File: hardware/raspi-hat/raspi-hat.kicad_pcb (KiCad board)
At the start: 2 copper layers, 41 parts, among them J1 Conn_02x05_Counter_Clockwise, J3 ATX-20, Q1 FDMS86101DC, Q2 FDMS86101DC, Q3 FDMS86101DC, Q4 FDMS86101DC, Q5 FDMS86101DC, Q6 FDMS86101DC, U1 STSPIN32G4, Y1 Crystal_GND23_Small

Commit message: updatd ioc
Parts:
- removed Q6: FDMS86101DC, Package_DFN_QFN:PQFN-8-EP_6x5mm_P1.27mm_Generic
- added D3: ER1Q-LTP, Diode_SMD:D_SMB, F.Cu at (43.3, 37.7)
- added J2: Conn_01x03_Pin, Connector_Phoenix_MC:PhoenixContact_MC_1,5_3-G-3.81_1x03_P3.81mm_Horizontal, F.Cu at (102.9, 124.7)
- added J4: Raspberry_Pi_4, Connector_PinSocket_2.54mm:PinSocket_2x20_P2.54mm_Vertical, B.Cu at (108.2, 105.0)
- added Q7: FDMS86101, Package_TO_SOT_SMD:TDSON-8-1, F.Cu at (120.0, 122.0)
- added R23: 0, Resistor_SMD:R_0603_1608Metric, F.Cu at (41.1, 41.7)
- added R24: 0, Resistor_SMD:R_0603_1608Metric, F.Cu at (41.1, 44.2)
- added REF**: MountingHole_3.2mm_M3, MountingHole:MountingHole_3.2mm_M3, F.Cu at (161.5, 152.8)
- added REF**: MountingHole_3.2mm_M3, MountingHole:MountingHole_3.2mm_M3, F.Cu at (161.5, 103.8)
- added REF**: MountingHole_3.2mm_M3, MountingHole:MountingHole_3.2mm_M3, F.Cu at (103.5, 103.8)
- added REF**: MountingHole_3.2mm_M3, MountingHole:MountingHole_3.2mm_M3, F.Cu at (103.5, 152.5)
- added RV1: 10k, Potentiometer_SMD:Potentiometer_Bourns_3224W_Vertical, F.Cu at (71.0, 123.0)
- Q1, Q2, Q3, Q4, Q5: value FDMS86101DC -> FDMS86101; footprint Package_DFN_QFN:PQFN-8-EP_6x5mm_P1.27mm_Generic -> Package_TO_SOT_SMD:TDSON-8-1
- moved Q2 108.3 mm to (120.0, 136.0), turned to 0 degrees
- moved Q3 105.5 mm to (112.0, 136.0), turned to 0 degrees
- moved Q1 103.7 mm to (120.0, 129.0), turned to 0 degrees
- moved Q4 95.8 mm to (112.0, 129.0), turned to 0 degrees
- moved C5 88.7 mm to (59.5, 72.5)
- moved C1 88.7 mm to (56.2, 96.5)
- moved C2 88.7 mm to (52.2, 92.5)
- moved C3 88.7 mm to (88.2, 78.0)
- moved C4 88.7 mm to (88.2, 80.5)
- moved C6 88.7 mm to (62.9, 72.5)
- moved C7 88.7 mm to (66.2, 72.5)
- moved C8 88.7 mm to (84.2, 100.5)
- moved D1 88.7 mm to (92.2, 79.5)
- moved J1 88.7 mm to (65.2, 102.5)
- moved R1 88.7 mm to (73.2, 48.5)
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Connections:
- net /controller/+3V3 renamed /+3V3
- C5 pad 2: /controller/inverter/OUT1 -> /controller/phase_u
- C6 pad 2: /controller/inverter/OUT3 -> /controller/phase_w
- C7 pad 2: /controller/inverter/OUT2 -> /controller/phase_v
- J1 pad 10: unconnected-(J1-Pin_10-Pad10) -> /controller/reset
- J1 pad 2: unconnected-(J1-Pin_2-Pad2) -> /controller/v_mc
- J1 pad 4: unconnected-(J1-Pin_4-Pad4) -> /controller/v_mc
- J1 pad 5: unconnected-(J1-Pin_5-Pad5) -> /controller/swd_io
- J1 pad 7: unconnected-(J1-Pin_7-Pad7) -> /controller/swd_clk
- J1 pad 9: unconnected-(J1-Pin_9-Pad9) -> /GND
- J3 pad 14: /power-supply/pwr_on -> /GND
- Q1 pad 1: /controller/inverter/OUT1 -> /controller/phase_v
- Q1 pad 2: /controller/inverter/LS1 -> /controller/phase_v
- Q1 pad 3: Net-(Q1-S) -> /controller/phase_v
- Q1 pad 4: (no net) -> /controller/inverter/HS2
- Q1 pad 5: (no net) -> /+12V
- Q2 pad 1: /controller/inverter/OUT2 -> /controller/phase_w
- Q2 pad 2: /controller/inverter/LS2 -> /controller/phase_w
- Q2 pad 3: Net-(Q2-S) -> /controller/phase_w
- Q2 pad 4: (no net) -> /controller/inverter/HS3
- Q2 pad 5: (no net) -> /+12V
- Q3 pad 1: /controller/inverter/OUT3 -> Net-(Q3-S-Pad1)
- Q3 pad 2: /controller/inverter/LS3 -> Net-(Q3-S-Pad1)
- Q3 pad 3: Net-(Q3-S) -> Net-(Q3-S-Pad1)
- Q3 pad 4: (no net) -> /controller/inverter/LS3
- Q3 pad 5: (no net) -> /controller/phase_w
- Q4 pad 1: /controller/+12V -> Net-(Q4-S-Pad1)
- Q4 pad 2: /controller/inverter/HS3 -> Net-(Q4-S-Pad1)
- Q4 pad 3: /controller/inverter/OUT3 -> Net-(Q4-S-Pad1)
- Q4 pad 4: (no net) -> /controller/inverter/LS2
- Q4 pad 5: (no net) -> /controller/phase_v
- Q5 pad 1: /controller/+12V -> Net-(Q5-S-Pad1)
- Q5 pad 2: /controller/inverter/HS2 -> Net-(Q5-S-Pad1)
- Q5 pad 3: /controller/inverter/OUT2 -> Net-(Q5-S-Pad1)
- Q5 pad 4: (no net) -> /controller/inverter/LS1
- Q5 pad 5: (no net) -> /controller/phase_u
- R1 pad 4: Net-(Q1-S) -> Net-(Q5-S-Pad1)
- R2 pad 4: Net-(Q2-S) -> Net-(Q4-S-Pad1)
- R21 pad 1: /controller/+12V -> /+12V
- R3 pad 4: Net-(Q3-S) -> Net-(Q3-S-Pad1)
- U1 pad 36: /controller/inverter/OUT3 -> /controller/phase_w
- U1 pad 39: /controller/inverter/OUT2 -> /controller/phase_v
- U1 pad 42: /controller/inverter/OUT1 -> /controller/phase_u
- U1 pad 45: unconnected-(U1-PA9-Pad45) -> /controller/uart_tx
- U1 pad 46: unconnected-(U1-PA10-Pad46) -> /controller/uart_rx
- U1 pad 49: unconnected-(U1-PA13-Pad49) -> /controller/swd_io
- U1 pad 50: unconnected-(U1-PA14-Pad50) -> /controller/swd_clk
- U1 pad 52: unconnected-(U1-SCREF-Pad52) -> Net-(U1-SCREF)
- U1 pad 53: /controller/pwr_on -> unconnected-(U1-PD2-Pad53)
- U1 pad 59: /controller/i2c_scl -> /controller/boot
- U1 pad 60: /controller/i2c_sda -> unconnected-(U1-PB9-Pad60)
- U1 pad 61: /controller/+12V -> /+12V
- U1 pad 64: /controller/+12V -> /+12V
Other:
- board outline added: 65 x 57 mm

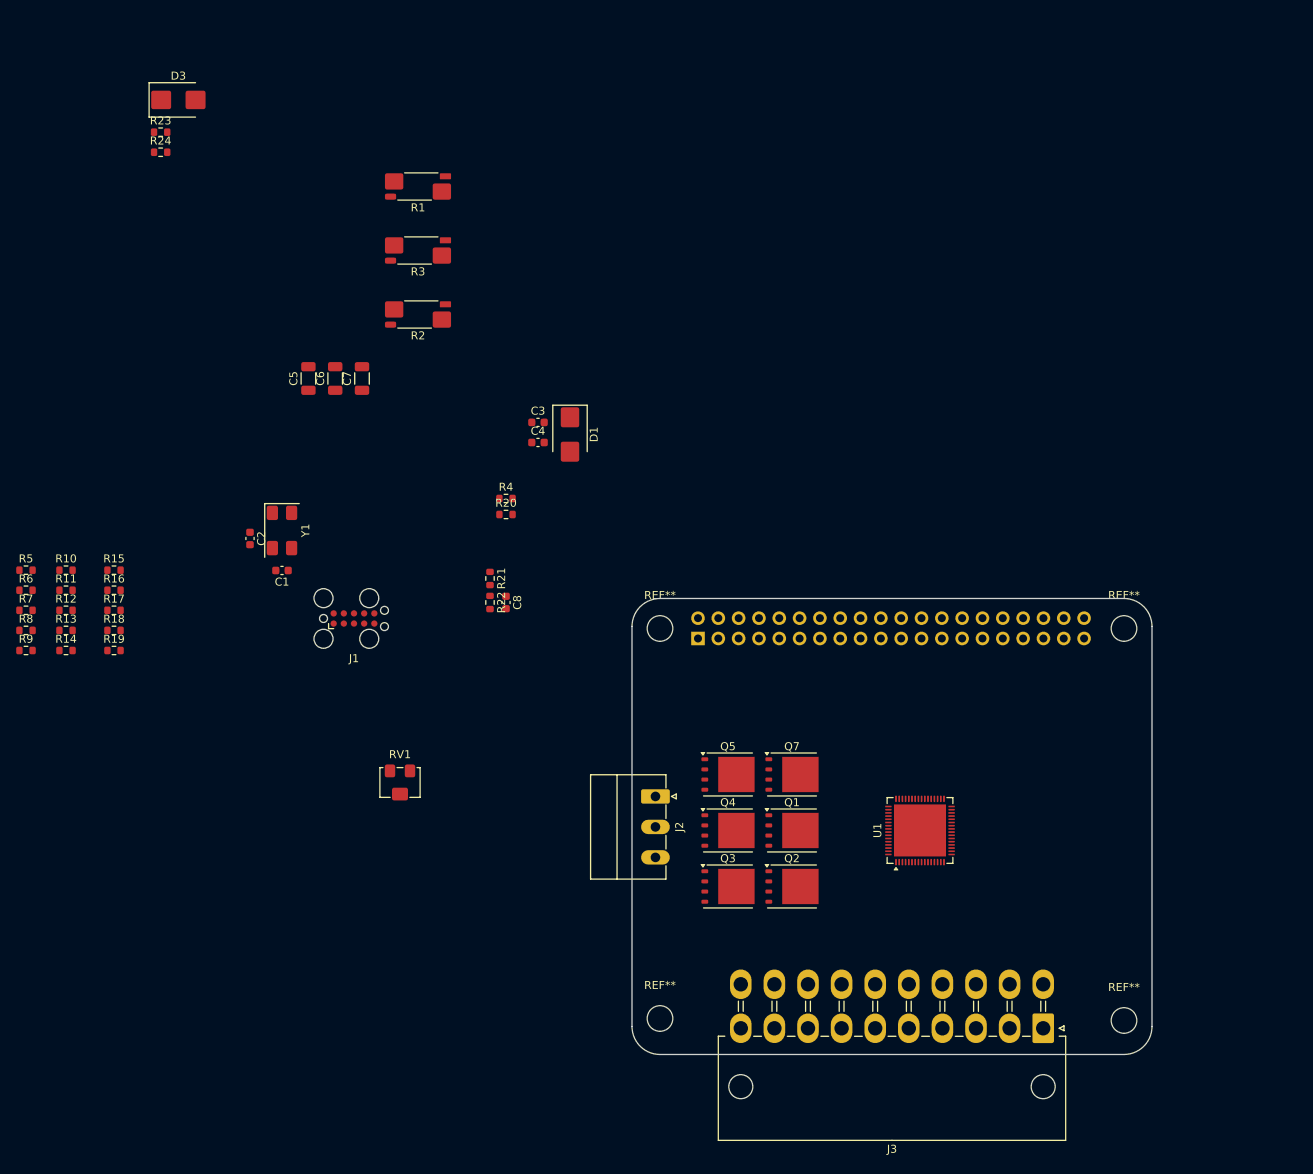
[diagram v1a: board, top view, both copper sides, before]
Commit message: added more parts
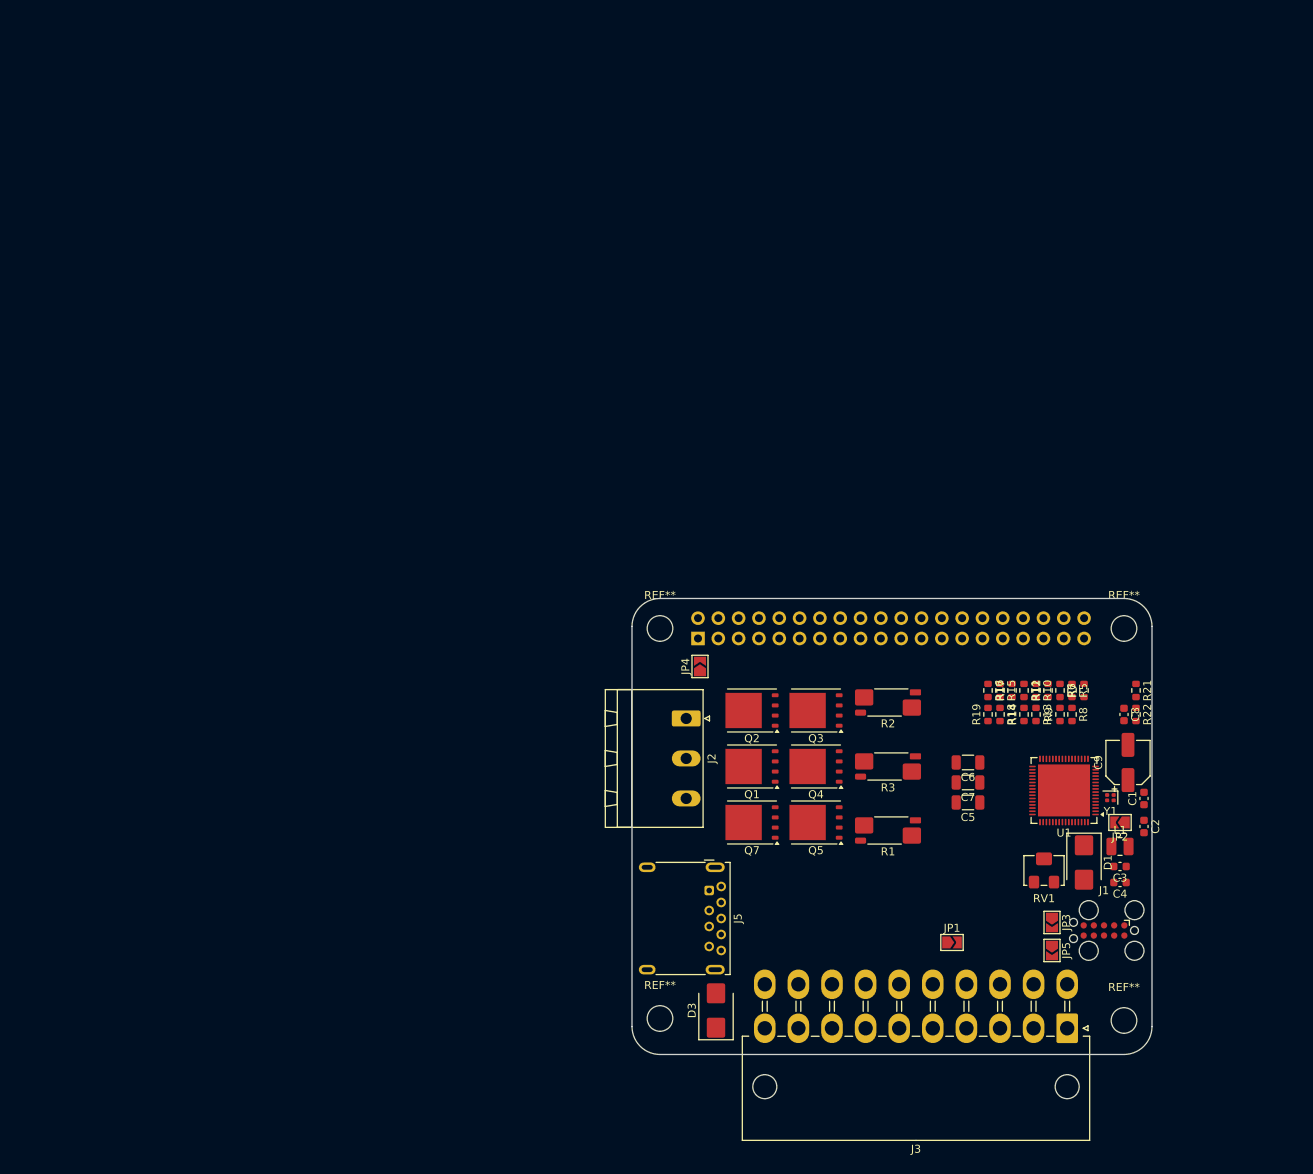
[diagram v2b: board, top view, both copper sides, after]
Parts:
- removed R20, R23, R24, R4: 0, Resistor_SMD:R_0603_1608Metric
- added C9: 25u, Capacitor_SMD:CP_Elec_5x5.3, F.Cu at (162.0, 120.5)
- added J5: USB3_A, Connector_USB:USB3_A_Molex_48393-001, F.Cu at (109.7, 136.5)
- added JP1: Jumper_2_Open, Jumper:SolderJumper-2_P1.3mm_Open_TrianglePad1.0x1.5mm, F.Cu at (140.0, 143.0)
- added JP2: Jumper_2_Open, Jumper:SolderJumper-2_P1.3mm_Open_TrianglePad1.0x1.5mm, F.Cu at (161.0, 128.0)
- added JP3: Jumper_2_Open, Jumper:SolderJumper-2_P1.3mm_Open_TrianglePad1.0x1.5mm, F.Cu at (152.5, 140.5)
- added JP4: Jumper_2_Open, Jumper:SolderJumper-2_P1.3mm_Open_TrianglePad1.0x1.5mm, F.Cu at (108.5, 108.5)
- added JP5: Jumper_2_Open, Jumper:SolderJumper-2_P1.3mm_Open_TrianglePad1.0x1.5mm, F.Cu at (152.5, 144.0)
- added L1: 15u, Inductor_SMD:L_1008_2520Metric, F.Cu at (161.0, 131.0)
- J2: footprint Connector_Phoenix_MC:PhoenixContact_MC_1,5_3-G-3.81_1x03_P3.81mm_Horizontal -> Connector_Phoenix_MSTB:PhoenixContact_MSTBA_2,5_3-G_1x03_P5.00mm_Horizontal
- Y1: footprint Crystal:Crystal_SMD_0603-4Pin_6.0x3.5mm -> Crystal:Crystal_SMD_1210-4Pin_1.2x1.0mm_RotB
- moved R7 132.6 mm to (156.5, 111.5), turned to 90 degrees
- moved D3 132.2 mm to (110.5, 151.5), turned to 90 degrees
- moved R5 131.6 mm to (155.0, 111.5), turned to -90 degrees
- moved R8 131.2 mm to (155.0, 114.5), turned to -90 degrees
- moved R6 129.9 mm to (153.5, 111.5), turned to -90 degrees
- moved R9 129.5 mm to (153.5, 114.5), turned to 90 degrees
- moved R12 123.2 mm to (152.0, 111.5), turned to 90 degrees
- moved R10 122.2 mm to (150.5, 111.5), turned to -90 degrees
- moved R13 121.7 mm to (150.5, 114.5), turned to -90 degrees
- moved R11 120.4 mm to (149.0, 111.5), turned to -90 degrees
- moved R14 120.0 mm to (149.0, 114.5), turned to 90 degrees
- moved C2 117.4 mm to (164.0, 128.5)
- moved R17 112.7 mm to (147.5, 111.5), turned to 90 degrees
- moved R15 111.8 mm to (146.0, 111.5), turned to -90 degrees
- moved C1 111.5 mm to (164.0, 125.0), turned to 90 degrees
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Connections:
- net /+3V3 renamed /controller/shunt-amp/+3V3
- J2 pad 1: /controller/phase_u -> /controller/phase_w
- J2 pad 3: /controller/phase_w -> /controller/phase_u
- J3 pad 14: /GND -> /controller/power_on
- U1 pad 3: unconnected-(U1-PC13-Pad3) -> /controller/hall_1
- U1 pad 4: unconnected-(U1-PC14-Pad4) -> /controller/hall_2
- U1 pad 5: unconnected-(U1-PC15-Pad5) -> /controller/hall_3
- U1 pad 53: unconnected-(U1-PD2-Pad53) -> /controller/power_on

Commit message: added some layers
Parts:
- JP1, JP2, JP3, JP4, JP5: moved to B.Cu
- Y1: footprint Crystal:Crystal_SMD_1210-4Pin_1.2x1.0mm_RotB -> Crystal:Crystal_SMD_3225-4Pin_3.2x2.5mm
- moved J1 27.3 mm to (152.5, 115.0), turned to 90 degrees
- moved J5 24.5 mm to (110.7, 112.0)
- moved R2 20.2 mm to (136.6, 132.6)
- moved J2 15.0 mm to (106.8, 130.0)
- moved D1 14.4 mm to (161.5, 146.5), turned to 0 degrees
- moved R1 13.9 mm to (136.6, 142.1)
- moved Q5 13.8 mm to (127.1, 141.1)
- moved Q7 13.8 mm to (119.1, 141.1)
- moved JP2 13.0 mm to (157.5, 140.5), turned to -90 degrees
- moved C1 11.6 mm to (162.5, 136.5), turned to 0 degrees
- moved R10 11.4 mm to (153.5, 122.5)
- moved R11 11.4 mm to (152.0, 122.5)
- moved R12 11.4 mm to (155.0, 122.5)
- moved R13 11.4 mm to (153.5, 125.5)
- moved R14 11.4 mm to (152.0, 125.5)
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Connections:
- Y1 pad 3: Net-(C1-Pad1) -> Net-(U1-PF0)
- Y1 pad 4: Net-(U1-PF0) -> Net-(C1-Pad1)
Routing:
- net /+5V: track 0.00 -> 110.2 mm
- net Net-(JP5-B): track 0.00 -> 13.5 mm
- net Net-(D3-A): track 0.00 -> 11.8 mm
- net /+12V: track 0.00 -> 7.50 mm
- net /controller/power_on: track 0.00 -> 5.38 mm
- net /+3V3: track 0.00 -> 5.29 mm
- net Net-(JP4-B): track 0.00 -> 3.12 mm
- net /controller/shunt-amp/+3V3: track 0.00 -> 1.79 mm
- net Net-(Q5-S-Pad1): vias 0 -> 70
- net Net-(Q4-S-Pad1): vias 0 -> 59
- net Net-(Q3-S-Pad1): vias 0 -> 74
- net /controller/phase_w: vias 0 -> 69
- net /controller/phase_v: vias 0 -> 61
- net /controller/phase_u: vias 0 -> 62
- net /GND: vias 0 -> 105
- added copper zone on F.Cu, net /+12V
- added copper zone on B.Cu, net /GND
- added copper zone on F.Cu, net /GND
- added copper zone on F.Cu, net /controller/phase_u
- added copper zone on In1.Cu, net /controller/phase_u
- added copper zone on In2.Cu, net /controller/phase_u
- added copper zone on F.Cu, net /controller/phase_v
- added copper zone on In1.Cu, net /controller/phase_v
- added copper zone on In2.Cu, net /controller/phase_v
- added copper zone on F.Cu, net /controller/phase_w
- added copper zone on In1.Cu, net /controller/phase_w
- added copper zone on In2.Cu, net /controller/phase_w
- added copper zone on F.Cu, net Net-(Q3-S-Pad1)
- added copper zone on In1.Cu, net Net-(Q3-S-Pad1)
- added copper zone on In2.Cu, net Net-(Q3-S-Pad1)
- added copper zone on F.Cu, net Net-(Q4-S-Pad1)
- added copper zone on In1.Cu, net Net-(Q4-S-Pad1)
- added copper zone on In2.Cu, net Net-(Q4-S-Pad1)
- added copper zone on F.Cu, net Net-(Q5-S-Pad1)
- added copper zone on In1.Cu, net Net-(Q5-S-Pad1)
- added copper zone on In2.Cu, net Net-(Q5-S-Pad1)
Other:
- copper layers 2 -> 4

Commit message: routing
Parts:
- moved C2 7.18 mm to (162.7, 137.7), turned to 180 degrees
- moved C1 4.91 mm to (162.7, 131.6), turned to 180 degrees
- moved C6 1.98 mm to (145.3, 128.4)
- moved C7 1.79 mm to (145.4, 131.2)
- moved C5 1.65 mm to (145.3, 134.6), turned to 180 degrees
- moved Y1 1.15 mm to (162.7, 134.6), turned to -90 degrees
- moved R9 0.05 mm to (156.4, 125.5)
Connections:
- JP2 pad 2: /controller/shunt-amp/+3V3 -> /controller/v_mc
- JP3 pad 1: /controller/shunt-amp/+3V3 -> /controller/v_mc
- R12 pad 2: /controller/shunt-amp/+3V3 -> /controller/v_mc
- R17 pad 2: /controller/shunt-amp/+3V3 -> /controller/v_mc
- R7 pad 2: /controller/shunt-amp/+3V3 -> /controller/v_mc
- RV1 pad 1: /controller/shunt-amp/+3V3 -> /controller/v_mc
- U1 pad 1: /controller/shunt-amp/+3V3 -> /controller/v_mc
- U1 pad 2: /controller/shunt-amp/+3V3 -> /controller/v_mc
- U1 pad 26: /controller/shunt-amp/+3V3 -> /controller/v_mc
- U1 pad 27: /controller/shunt-amp/+3V3 -> /controller/v_mc
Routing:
- net /+3V3: track 5.29 -> 102.6 mm, vias 0 -> 3
- net /+12V: track 7.50 -> 92.4 mm, vias 0 -> 3
- net /controller/hall_1: track 0.00 -> 79.7 mm, vias 0 -> 2
- net /controller/hall_2: track 0.00 -> 79.0 mm, vias 0 -> 2
- net /controller/hall_3: track 0.00 -> 77.6 mm, vias 0 -> 2
- net /controller/boot: track 0.00 -> 75.2 mm, vias 0 -> 2
- net /controller/uart_rx: track 0.00 -> 64.8 mm, vias 0 -> 3
- net /controller/uart_tx: track 0.00 -> 62.1 mm, vias 0 -> 3
- net /controller/v_mc: track 0.00 -> 61.1 mm, vias 0 -> 6
- net /controller/reset: track 0.00 -> 59.9 mm, vias 0 -> 3
- net /controller/shunt1_h: track 0.00 -> 52.0 mm, vias 0 -> 2
- net /controller/inverter/HS3: track 0.00 -> 48.8 mm, vias 0 -> 2
- net /controller/swd_io: track 0.00 -> 45.9 mm, vias 0 -> 2
- net /controller/inverter/LS3: track 0.00 -> 39.7 mm, vias 0 -> 2
- net /controller/swd_clk: track 0.00 -> 39.5 mm, vias 0 -> 2
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
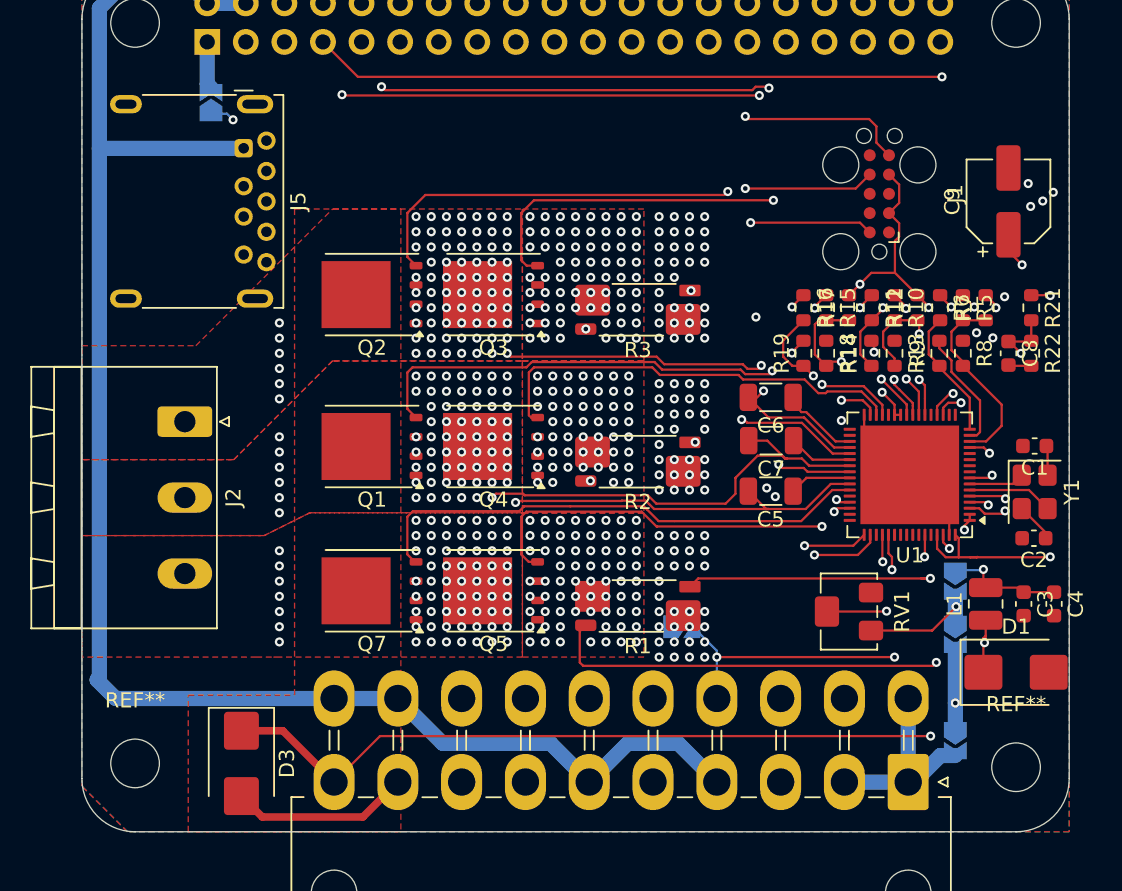
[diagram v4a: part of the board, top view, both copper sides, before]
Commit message: - added more gnd vias - all connected now. routing done
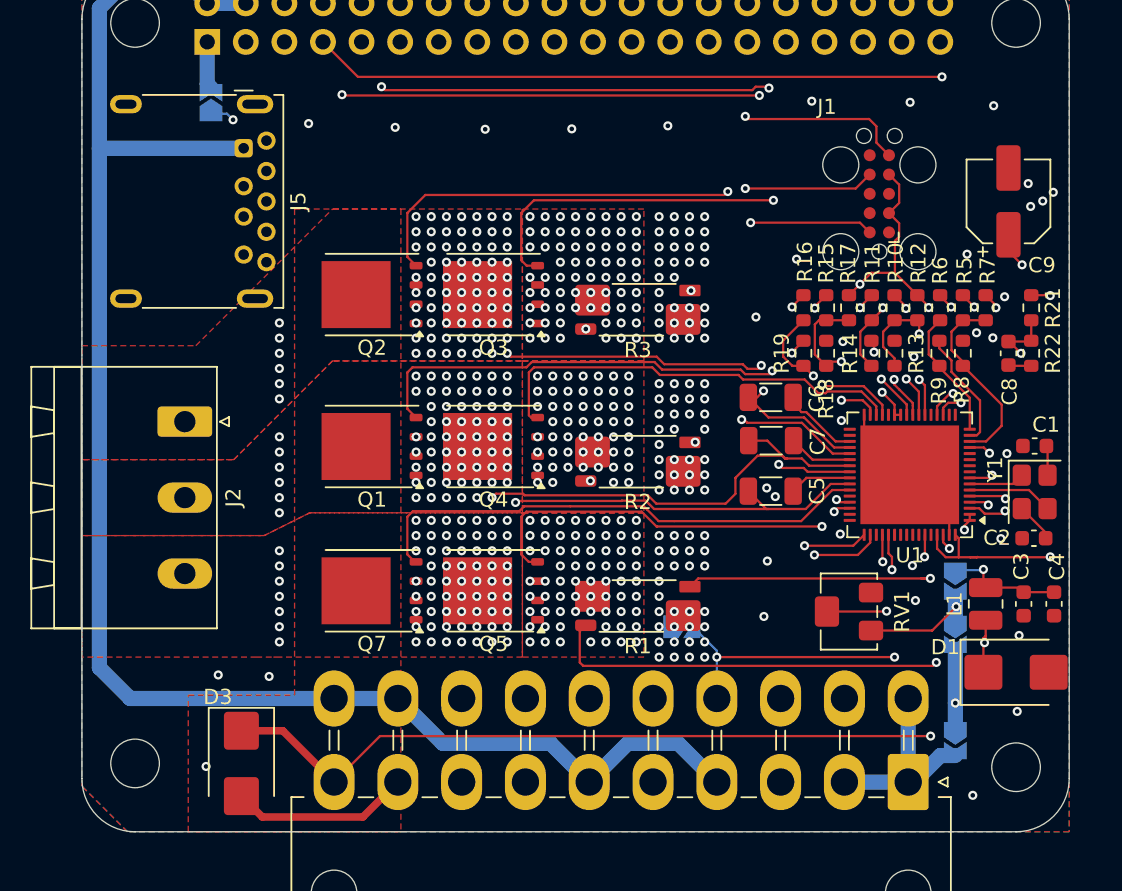
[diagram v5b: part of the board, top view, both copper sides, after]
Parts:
- RV1: value 10k -> 50k
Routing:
- net /controller/shunt-amp1/OP-: track 23.2 -> 22.2 mm
- net /+5V: track 110.2 -> 109.5 mm
- net /GND: vias 89 -> 114
